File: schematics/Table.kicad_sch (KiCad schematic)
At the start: 9 parts, among them J10 WF-2, Q7 2N7002

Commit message: Файлы измененный Kicad
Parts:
- renumbered C28 to C0500, D7 to LD0500, Q7 to Q0500, R30 to R0500, R29 to R0501, R26 to R0502, R27 to R0503, R28 to R0504
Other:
- moved on the sheet: C0500
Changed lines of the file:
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@@
 	(wire
 		(pts
-			(xy 113.03 81.28) (xy 124.46 81.28)
+			(xy 113.03 81.28) (xy 127 81.28)
 		)
 		(stroke
@@
 	(wire
 		(pts
-			(xy 124.46 83.82) (xy 124.46 81.28)
-		)
-		(stroke
-			(width 0)
-			(type default)
-		)
-	)
-	(wire
-		(pts
-			(xy 124.46 91.44) (xy 124.46 93.98)
+			(xy 127 83.82) (xy 127 81.28)
+		)
+		(stroke
+			(width 0)
+			(type default)
+		)
+	)
+	(wire
+		(pts
+			(xy 127 91.44) (xy 127 93.98)
 		)
 		(stroke
@@
 	(wire
 		(pts
-			(xy 124.46 93.98) (xy 113.03 93.98)
+			(xy 127 93.98) (xy 113.03 93.98)
 		)
 		(stroke
@@
 		(dnp no)
 		(fields_autoplaced yes)
-		(property "Reference" "R26"
+		(property "Reference" "R0502"
 			(at 189.23 109.2199 0)
 			(effects
@@
 			(project "MasterBoard"
 				(path "/97e8f341-b455-4614-ab7f-cc310164e7aa/e30e4f09-c240-4d68-a862-af3d4cc81fa3"
-					(reference "R26")
+					(reference "R0502")
 					(unit 1)
 				)
@@
 		(dnp no)
 		(fields_autoplaced yes)
-		(property "Reference" "Q7"
+		(property "Reference" "Q0500"
 			(at 210.82 102.8699 0)
 			(effects
@@
 			(project "MasterBoard"
 				(path "/97e8f341-b455-4614-ab7f-cc310164e7aa/e30e4f09-c240-4d68-a862-af3d4cc81fa3"
-					(reference "Q7")
+					(reference "Q0500")
 					(unit 1)
 				)
@@
 		(dnp no)
 		(fields_autoplaced yes)
-		(property "Reference" "R29"
+		(property "Reference" "R0501"
 			(at 194.31 99.06 90)
 			(effects
@@
 			(project "MasterBoard"
 				(path "/97e8f341-b455-4614-ab7f-cc310164e7aa/e30e4f09-c240-4d68-a862-af3d4cc81fa3"
-					(reference "R29")
+					(reference "R0501")
 					(unit 1)
 				)
@@
 		(dnp no)
 		(fields_autoplaced yes)
-		(property "Reference" "R28"
+		(property "Reference" "R0504"
 			(at 115.57 97.7899 0)
 			(effects
@@
 			(project "MasterBoard"
 				(path "/97e8f341-b455-4614-ab7f-cc310164e7aa/e30e4f09-c240-4d68-a862-af3d4cc81fa3"
-					(reference "R28")
+					(reference "R0504")
 					(unit 1)
 				)
@@
 		(dnp no)
 		(fields_autoplaced yes)
-		(property "Reference" "D7"
+		(property "Reference" "LD0500"
 			(at 210.82 85.4074 90)
 			(effects
@@
 			(project "MasterBoard"
 				(path "/97e8f341-b455-4614-ab7f-cc310164e7aa/e30e4f09-c240-4d68-a862-af3d4cc81fa3"
-					(reference "D7")
+					(reference "LD0500")
 					(unit 1)
 				)
@@
 		(dnp no)
 		(fields_autoplaced yes)
-		(property "Reference" "R27"
+		(property "Reference" "R0503"
 			(at 116.84 86.3599 0)
 			(effects
@@
 			(project "MasterBoard"
 				(path "/97e8f341-b455-4614-ab7f-cc310164e7aa/e30e4f09-c240-4d68-a862-af3d4cc81fa3"
-					(reference "R27")
+					(reference "R0503")
 					(unit 1)
 				)
@@
 	(symbol
 		(lib_id "Device:C")
-		(at 124.46 87.63 0)
-		(unit 1)
-		(exclude_from_sim no)
-		(in_bom yes)
-		(on_board yes)
-		(dnp no)
-		(fields_autoplaced yes)
-		(property "Reference" "C28"
-			(at 128.27 86.3599 0)
+		(at 127 87.63 0)
+		(unit 1)
+		(exclude_from_sim no)
+		(in_bom yes)
+		(on_board yes)
+		(dnp no)
+		(fields_autoplaced yes)
+		(property "Reference" "C0500"
+			(at 130.81 86.3599 0)
 			(effects
 				(font
@@
 		)
 		(property "Value" "100n"
-			(at 128.27 88.8999 0)
+			(at 130.81 88.8999 0)
 			(effects
 				(font
@@
 		)
 		(property "Footprint" "Capacitor_SMD:C_0805_2012Metric"
-			(at 125.4252 91.44 0)
+			(at 127.9652 91.44 0)
 			(effects
 				(font
@@
 		)
 		(property "Datasheet" "~"
-			(at 124.46 87.63 0)
+			(at 127 87.63 0)
 			(effects
 				(font
@@
 		)
 		(property "Description" "Unpolarized capacitor"
-			(at 124.46 87.63 0)
+			(at 127 87.63 0)
 			(effects
 				(font
@@
 			(project "MasterBoard"
 				(path "/97e8f341-b455-4614-ab7f-cc310164e7aa/e30e4f09-c240-4d68-a862-af3d4cc81fa3"
-					(reference "C28")
+					(reference "C0500")
 					(unit 1)
 				)
@@
 		(dnp no)
 		(fields_autoplaced yes)
-		(property "Reference" "R30"
+		(property "Reference" "R0500"
 			(at 209.55 92.7099 0)
 			(effects
@@
 			(project "MasterBoard"
 				(path "/97e8f341-b455-4614-ab7f-cc310164e7aa/e30e4f09-c240-4d68-a862-af3d4cc81fa3"
-					(reference "R30")
-					(unit 1)
-				)
+					(reference "R0500")
+					(unit 1)
+				)

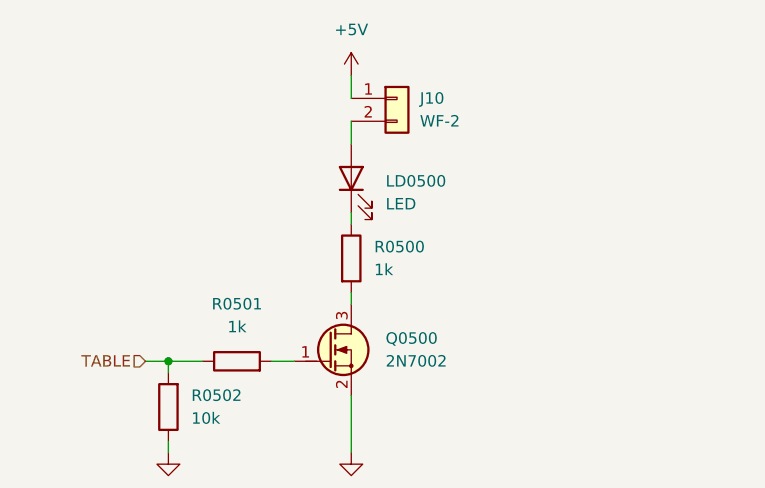
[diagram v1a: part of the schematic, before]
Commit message: Прошелся по всей схеме: 1. почистил компоненты; 2. задал посадочные места; 3. Выставил все ссылки на плате в притык, дальнейшее расширение - смена мк
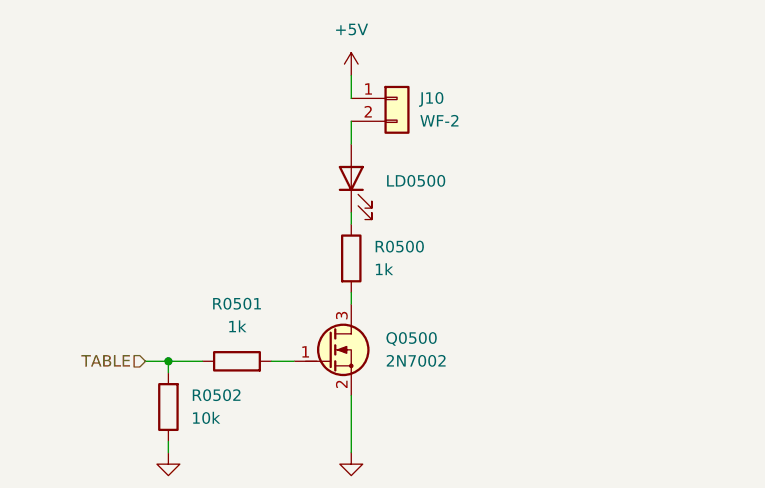
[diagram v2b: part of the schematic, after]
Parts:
- LD0500: value LED -> ~
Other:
- company: (none) -> Филимонов и К
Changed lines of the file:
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@@
 	(title_block
 		(date "2025-02-25")
+		(company "Филимонов и К")
 		(comment 1 "Термо стол")
 		(comment 2 "Филимонов С.В.")
@@
 			)
 		)
-		(property "Value" "LED"
+		(property "Value" "~"
 			(at 210.82 87.9474 90)
 			(effects

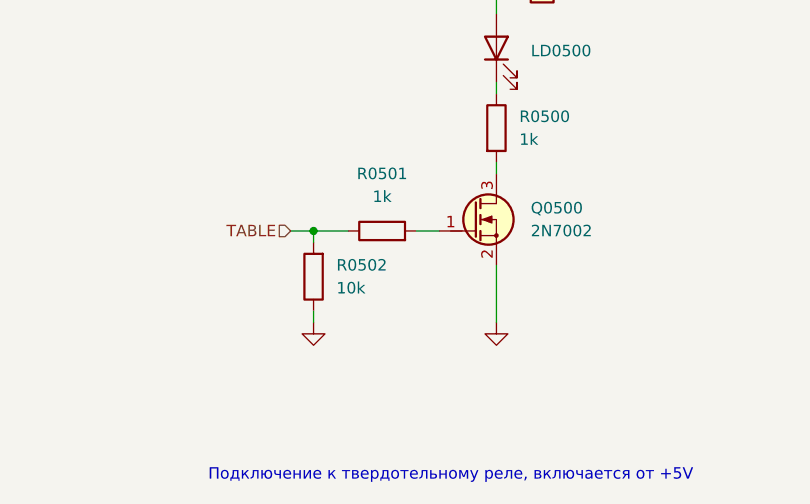
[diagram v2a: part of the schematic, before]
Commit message: Не корректно посадочное место выбрал
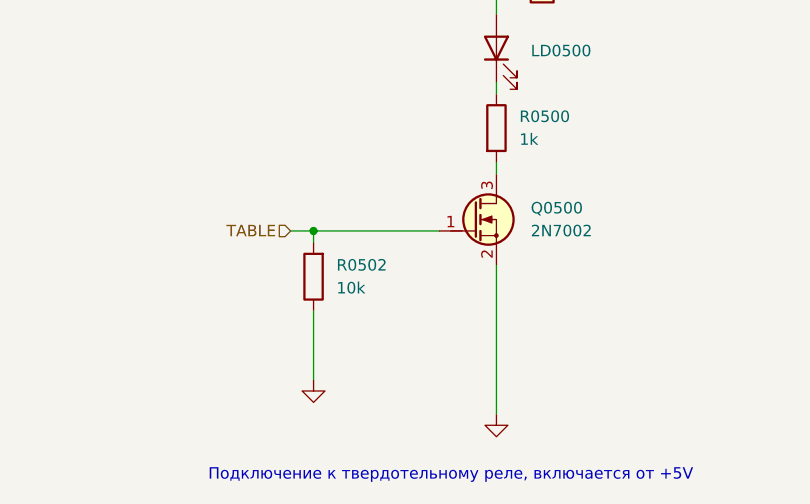
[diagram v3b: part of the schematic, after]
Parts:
- removed R0501: 1k, Resistor_SMD:R_0805_2012Metric, symbol Device:R
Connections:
- net TABLE: now also Q0500.1 (G)
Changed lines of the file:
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@@
-	(wire
-		(pts
-			(xy 198.12 105.41) (xy 200.66 105.41)
-		)
-		(stroke
-			(width 0)
-			(type default)
-		)
-	)
 	(wire
 		(pts
@@
 	(wire
 		(pts
-			(xy 186.69 114.3) (xy 186.69 115.57)
+			(xy 186.69 114.3) (xy 186.69 121.92)
 		)
 		(stroke
@@
 	(wire
 		(pts
-			(xy 207.01 109.22) (xy 207.01 115.57)
+			(xy 207.01 109.22) (xy 207.01 125.73)
 		)
 		(stroke
@@
 	(wire
 		(pts
-			(xy 190.5 105.41) (xy 186.69 105.41)
+			(xy 186.69 105.41) (xy 200.66 105.41)
 		)
 		(stroke
@@
 	(symbol
 		(lib_id "power:GND")
-		(at 207.01 115.57 0)
+		(at 207.01 125.73 0)
 		(unit 1)
 		(exclude_from_sim no)
@@
 		(fields_autoplaced yes)
 		(property "Reference" "#PWR0113"
-			(at 207.01 121.92 0)
+			(at 207.01 132.08 0)
 			(effects
 				(font
@@
 		)
 		(property "Value" "GND"
-			(at 207.01 120.65 0)
+			(at 207.01 130.81 0)
 			(effects
 				(font
@@
 		)
 		(property "Footprint" ""
-			(at 207.01 115.57 0)
+			(at 207.01 125.73 0)
 			(effects
 				(font
@@
 		)
 		(property "Datasheet" ""
-			(at 207.01 115.57 0)
+			(at 207.01 125.73 0)
 			(effects
 				(font
@@
 		)
 		(property "Description" "Power symbol creates a global label with name \"GND\" , ground"
-			(at 207.01 115.57 0)
+			(at 207.01 125.73 0)
 			(effects
 				(font
@@
 	)
 	(symbol
-		(lib_id "Device:R")
-		(at 194.31 105.41 90)
-		(unit 1)
-		(exclude_from_sim no)
-		(in_bom yes)
-		(on_board yes)
-		(dnp no)
-		(fields_autoplaced yes)
-		(property "Reference" "R0501"
-			(at 194.31 99.06 90)
-			(effects
-				(font
-					(size 1.27 1.27)
-				)
-			)
-		)
-		(property "Value" "1k"
-			(at 194.31 101.6 90)
-			(effects
-				(font
-					(size 1.27 1.27)
-				)
-			)
-		)
-		(property "Footprint" "Resistor_SMD:R_0805_2012Metric"
-			(at 194.31 107.188 90)
-			(effects
-				(font
-					(size 1.27 1.27)
-				)
-				(hide yes)
-			)
-		)
-		(property "Datasheet" "~"
-			(at 194.31 105.41 0)
-			(effects
-				(font
-					(size 1.27 1.27)
-				)
-				(hide yes)
-			)
-		)
-		(property "Description" "Resistor"
-			(at 194.31 105.41 0)
-			(effects
-				(font
-					(size 1.27 1.27)
-				)
-				(hide yes)
-			)
-		)
-		(pin "1"
-		)
-		(pin "2"
-		)
-		(instances
-			(project "MasterBoard"
-				(path "/97e8f341-b455-4614-ab7f-cc310164e7aa/e30e4f09-c240-4d68-a862-af3d4cc81fa3"
-					(reference "R0501")
-					(unit 1)
-				)
-			)
-		)
-	)
-	(symbol
 		(lib_id "power:GND")
-		(at 186.69 115.57 0)
+		(at 186.69 121.92 0)
 		(unit 1)
 		(exclude_from_sim no)
@@
 		(fields_autoplaced yes)
 		(property "Reference" "#PWR0109"
+			(at 186.69 128.27 0)
+			(effects
+				(font
+					(size 1.27 1.27)
+				)
+				(hide yes)
+			)
+		)
+		(property "Value" "GND"
+			(at 186.69 127 0)
+			(effects
+				(font
+					(size 1.27 1.27)
+				)
+				(hide yes)
+			)
+		)
+		(property "Footprint" ""
 			(at 186.69 121.92 0)
 			(effects
@@
 			)
 		)
-		(property "Value" "GND"
-			(at 186.69 120.65 0)
-			(effects
-				(font
-					(size 1.27 1.27)
-				)
-				(hide yes)
-			)
-		)
-		(property "Footprint" ""
-			(at 186.69 115.57 0)
-			(effects
-				(font
-					(size 1.27 1.27)
-				)
-				(hide yes)
-			)
-		)
 		(property "Datasheet" ""
-			(at 186.69 115.57 0)
+			(at 186.69 121.92 0)
 			(effects
 				(font
@@
 		)
 		(property "Description" "Power symbol creates a global label with name \"GND\" , ground"
-			(at 186.69 115.57 0)
-			(effects
-				(font
+			(at 186.69 121.92 0)
+			(effects
+				(font
